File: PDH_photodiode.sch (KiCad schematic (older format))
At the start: 23 parts, among them J1 CONN_01X03, J2 CONN_01X02, U1 LT3032-5, U2 LTC6269

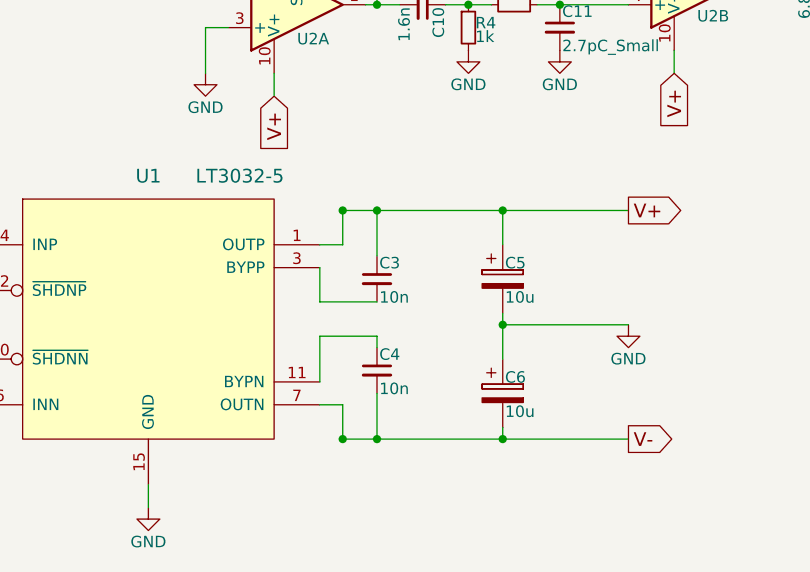
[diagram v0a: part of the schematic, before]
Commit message: LT3032
Replaced LT3032-05 with variable version
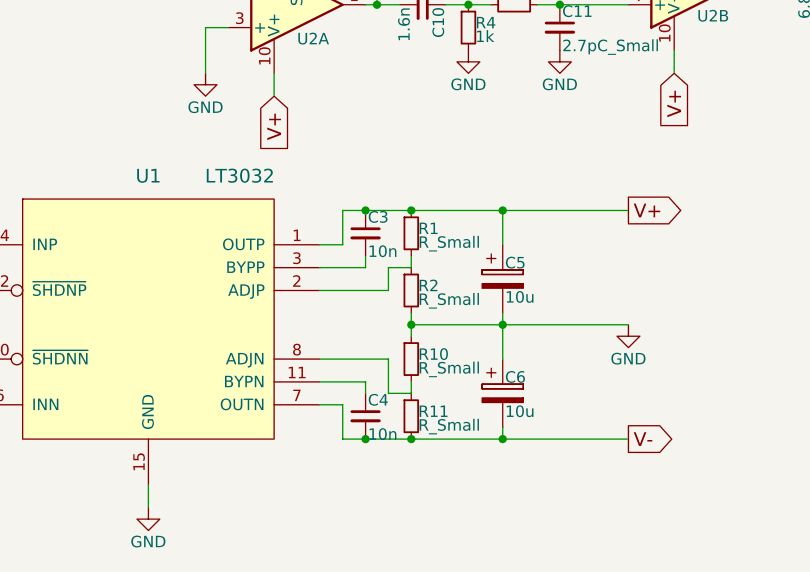
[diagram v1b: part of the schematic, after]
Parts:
- removed U1: LT3032-5, custom_Patrick_Baus:DFN-14-1EP_3x4mm_Pitch0.5mm_2Pads, symbol LT3032-X
- added R1, R10, R11, R2: R_Small, Resistors_SMD:R_0603, symbol R_Small
- added U1: LT3032, symbol LT3032
- U2: footprint Housings_DFN_QFN:DFN-10-1EP_3x3mm_Pitch0.5mm -> (none)
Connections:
- net GND: now also R10.1, R2.2, U1.15 (GND), U1.4, U1.5
- net INN: now also U1.10 (~SHDNN), U1.16 (INN), U1.6 (INN), U1.9 (INN)
- net V+: now also R1.1, U1.1 (OUTP)
- net V-: now also R11.2, U1.7 (OUTN)
- net at C1.1, J1.1 (P1): now also U1.12 (~SHDNP), U1.14 (INP)
- net at C3.2: now also U1.3 (BYPP)
- net at C4.1: now also U1.11 (BYPN)
- new net: R1.2, R2.1, U1.2 (ADJP)
- new net: R10.2, R11.1, U1.8 (ADJN)
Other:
- moved on the sheet: C3, C4

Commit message: Revision 1.1
-Add DC output
-Fit board in a box
  (RND 455-00367)
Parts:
- removed C10: 1.6n, Capacitors_SMD:C_0805, symbol C_Small
- removed C11: 2.7pC_Small, Capacitors_SMD:C_0805, symbol C_Small
- removed C12: 6.8n, Capacitors_SMD:C_0805, symbol C_Small
- removed C13: 75p, Capacitors_SMD:C_0805, symbol C_Small
- removed C5, C6: 10u, Capacitors_Tantalum_SMD:CP_Tantalum_Case-D_EIA-7343-31_Reflow, symbol CP
- removed D1: S9055, PDH_photodiode:PhotoDiode_S9055, symbol S9055
- removed R1, R10, R11, R2: R_Small, Resistors_SMD:R_0603, symbol R_Small
- removed R4, R5: 1k, Resistors_SMD:R_0805, symbol R_Small
- removed R6: 100, Resistors_SMD:R_0603, symbol R_Small
- removed R7: 910, Resistors_SMD:R_0603, symbol R_Small
- removed R8, R9: 49.9, Resistors_SMD:R_0805, symbol R_Small
- removed U1: LT3032, symbol LT3032
- removed U2: LTC6269, symbol LTC6269
- added C10, C11, C8: DNF, Capacitor_SMD:C_0603_1608Metric, symbol Device:C_Small
- added C12: 100n, Capacitor_SMD:C_0603_1608Metric, symbol Device:C_Small
- added C5, C6: 10u, Capacitor_SMD:C_1210_3225Metric, symbol Device:C_Small
- added C7: 1.6n/C0G, Capacitor_SMD:C_0603_1608Metric, symbol Device:C_Small
- added D1: S9055, footprints:TO-18-3_mod, symbol Sensor_Optical:S5971
- added H1, H2: MountingHole, MountingHole:MountingHole_4.3mm_M4_DIN965, symbol Mechanical:MountingHole
- added J3: DC Out, Connector_Coaxial:SMA_Amphenol_901-144_Vertical, symbol Connector:Conn_Coaxial
- added LOGO1: Logo_APQ, footprints:APQ-Logo, symbol Custom_logos:Logo_APQ
- added LOGO2: Logo_ROHS, Symbol:RoHS-Logo_6mm_SilkScreen, symbol Custom_logos:Logo_ROHS
- added LOGO3: Logo_Open_Hardware_Small, Symbol:OSHW-Logo_5.7x6mm_SilkScreen, symbol Graphic:Logo_Open_Hardware_Small
- added R1: 1k, Resistor_SMD:R_0603_1608Metric, symbol Device:R_Small
- added R10: 200, Resistor_SMD:R_0603_1608Metric, symbol Device:R_Small
- added R11, R4: 49.9, Resistor_SMD:R_1206_3216Metric, symbol Device:R_Small
- added R2, R7: 105k, Resistor_SMD:R_0603_1608Metric, symbol Device:R_Small
- added R5, R6: 100k, Resistor_SMD:R_0603_1608Metric, symbol Device:R_Small
- added R8: 0, Resistor_SMD:R_0603_1608Metric, symbol Device:R_Small
- added R9: 10, Resistor_SMD:R_0603_1608Metric, symbol Device:R_Small
- added U1: LT3032, Package_DFN_QFN:Linear_DE14MA, symbol Regulator_Linear:LT3032
- added U2: LTC6269-10, Package_DFN_QFN:DFN-10-1EP_3x3mm_P0.5mm_EP1.65x2.38mm, symbol Amplifier_Operational:LTC6229xDD
- C1, C2: footprint Capacitors_SMD:C_1210 -> Capacitor_SMD:C_1210_3225Metric; symbol C_Small -> Device:C_Small; MFN (none) -> Taiyo Yuden; PN (none) -> GMK325BJ106MN-T
- C3, C4: footprint Capacitors_SMD:C_0603 -> Capacitor_SMD:C_0603_1608Metric; symbol C_Small -> Device:C_Small; MFN (none) -> Murata Electronics; PN (none) -> GRM1885C1H103JA01D
- C9: footprint Capacitors_SMD:C_1206 -> Capacitor_SMD:C_0603_1608Metric; symbol C_Small -> Device:C_Small; MFN (none) -> Wurth Electronics; PN (none) -> 885012206071
- J1: value CONN_01X03 -> ±5V-Supply; footprint Pin_Headers:Pin_Header_Straight_1x03_Pitch2.54mm -> Connector_PinHeader_2.54mm:PinHeader_1x03_P2.54mm_Vertical; symbol CONN_01X03 -> Connector_Generic:Conn_01x03; Config (none) -> DNF
- J2: value CONN_01X02 -> AC Out; footprint Connectors:SMA_THT_Jack_Straight -> Connector_Coaxial:SMA_Amphenol_132203-12_Horizontal; symbol CONN_01X02 -> Connector:Conn_Coaxial; Config (none) -> DNF; MFN (none) -> Amphenol; PN (none) -> 901-143-6RFX
- R3: value 50k -> 10k; footprint Resistors_SMD:R_0603 -> footprints:R_0603_1608Metric_mod; symbol R_Small -> Device:R_Small; MFN (none) -> Susumu
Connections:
- net GND: now also C10.2, C11.2, C12.1, C5.2, C6.1, C8.2, D1.2 (C), J3.2 (Ext), R1.1, R5.2, R6.1, R9.1, U1.4 (GND), U1.5 (GND), U2.2 (-)
- net V+: now also C12.2, C5.1, R2.1, U1.1 (OUTP), U2.10 (V+)
- net V-: now also C6.2, D1.3 (A), R7.2, U1.7 (OUTN), U2.11 (V-), U2.4 (V-)
- net at C1.1, J1.1 (Pin_1): now also U1.12 (~SHDNP), U1.14 (INP)
- net at C3.2: now also U1.3 (BYPP)
- net at C4.1: now also U1.11 (BYPN)
- net at J2.1 (In): now also C10.1, R4.1
- net at R3.1: now also C7.2, R11.2, U2.1
- net at R3.2: now also D1.1 (K), U2.3 (+)
- net INN: no longer names the net of C2.2, J1.3 (Pin_3)
- net INN: now also U1.10 (~SHDNN), U1.6 (INN), U1.9 (INN)
- new net: R10.2, R4.2, U2.9
- new net: R2.2, R5.1, U1.2 (ADJP)
- new net: R6.2, R7.1, U1.8 (ADJN)
- new net: C8.1, R8.2, U2.7 (+)
- new net: R10.1, R9.2, U2.8 (-)
- new net: C7.1, R1.2, R8.1
- new net: C11.1, J3.1 (In), R11.1
- no-connect marks 0 -> 2
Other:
- note added: "See README for alternative gain (R3)"
- note added: "The footprint pad size for D1 and R3 has been reduced\nin order to reduce parasitic capacitance. Do not use too much solder paste \nand clean carefully after assembly.\n"
- note added: "Use C8 (and R8) and C10 (and R4)\nfor optional low pass filtering."
- moved on the sheet: C1, C2, C3, C4, C9, R3

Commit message: Add README
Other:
- note added: "Use C1 (and R11) for \noptional low pass filtering."
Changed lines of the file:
@@
 NoConn ~ 4600 2650
 NoConn ~ 7850 2750
+Text Notes 6300 900  0    60   ~ 0
+Use C1 (and R11) for \noptional low pass filtering.
 $EndSCHEMATC

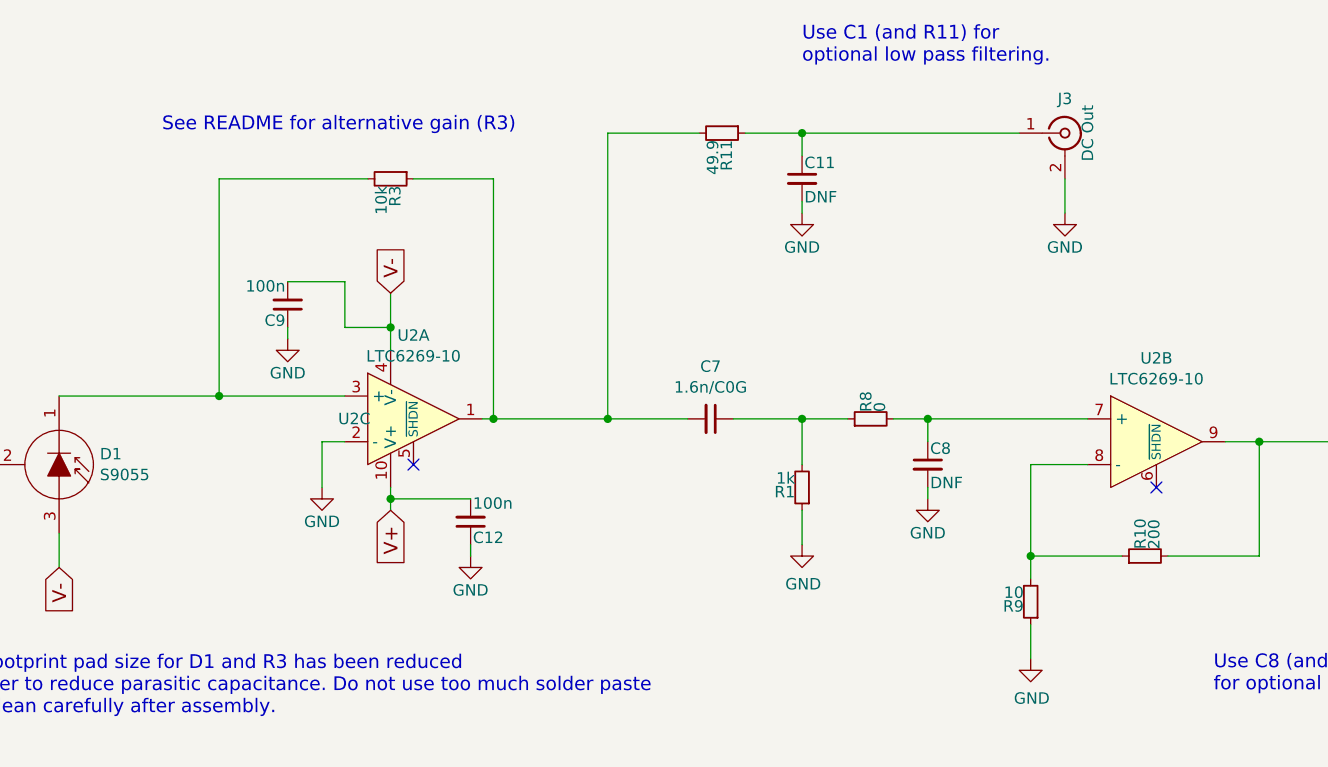
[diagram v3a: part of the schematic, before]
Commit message: Fix: Swap inverting and non-inverting input of TIA
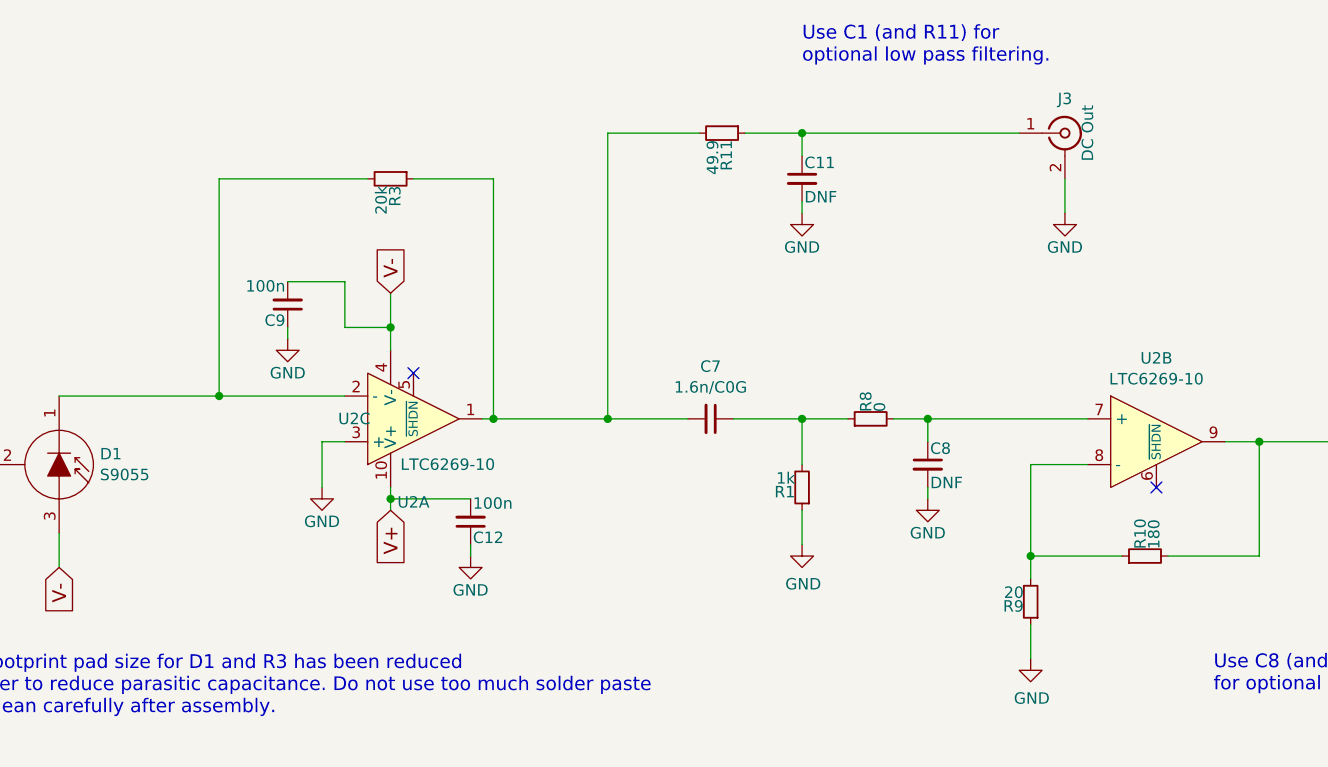
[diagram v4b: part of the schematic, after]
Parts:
- R10: value 200 -> 180
- R3: value 10k -> 20k
- R9: value 10 -> 20
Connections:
- net GND: now also U2.3 (+); no longer U2.2 (-)
- net at D1.1 (K), R3.2: now also U2.2 (-); no longer U2.3 (+)
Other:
- note removed: "See README for alternative gain (R3)"
- moved on the sheet: U2A
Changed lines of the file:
@@
 P 4500 1400
 F 0 "R3" H 4530 1420 50  0000 L CNN
-F 1 "10k" H 4530 1360 50  0000 L CNN
+F 1 "20k" H 4530 1360 50  0000 L CNN
 F 2 "footprints:R_0603_1608Metric_mod" H 4500 1400 50  0001 C CNN
 F 3 "" H 4500 1400 50  0001 C CNN
@@
 P 4600 2450
 F 0 "U2" H 4600 2815 50  0000 C CNN
-F 1 "LTC6269-10" H 4600 2724 50  0000 C CNN
+F 1 "LTC6269-10" H 4750 2650 50  0000 C CNN
 F 2 "Package_DFN_QFN:DFN-10-1EP_3x3mm_P0.5mm_EP1.65x2.38mm" H 4600 2050 50  0001 C CNN
 F 3 "" H 4600 2450 50  0001 C CNN
 	1    4600 2450
-	1    0    0    -1
+	1    0    0    1
 $EndComp
 $Comp
@@
 P 7300 3250
 F 0 "R9" H 7330 3270 50  0000 L CNN
-F 1 "10" H 7330 3210 50  0000 L CNN
+F 1 "20" H 7330 3210 50  0000 L CNN
 F 2 "Resistor_SMD:R_0603_1608Metric" H 7300 3250 50  0001 C CNN
 F 3 "" H 7300 3250 50  0001 C CNN
@@
 P 7800 3050
 F 0 "R10" H 7830 3070 50  0000 L CNN
-F 1 "200" H 7830 3010 50  0000 L CNN
+F 1 "180" H 7830 3010 50  0000 L CNN
 F 2 "Resistor_SMD:R_0603_1608Metric" H 7800 3050 50  0001 C CNN
 F 3 "" H 7800 3050 50  0001 C CNN
@@
 Text Notes 2550 3750 0    60   ~ 0
 The footprint pad size for D1 and R3 has been reduced\nin order to reduce parasitic capacitance. Do not use too much solder paste  \nand clean carefully after assembly.\n
-Text Notes 3500 1200 0    60   ~ 0
-See README for alternative gain (R3)
 Wire Wire Line
 	4500 2800 4850 2800
-NoConn ~ 4600 2650
+NoConn ~ 4600 2250
 NoConn ~ 7850 2750
 Text Notes 6300 900  0    60   ~ 0

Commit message: Update BOM and gerber files
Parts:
- C1, C2, C5, C6: PN GMK325BJ106MN-T -> UMR325AC7106MM-P
- C7: value 1.6n/C0G -> 10n; MFN (none) -> Murata Electronics; PN (none) -> GRM1885C1H103JA01D
- D1: Config (none) -> DNF
- J2: Config DNF -> (none)
- R1: MFN Susumu -> Yageo; PN (none) -> RT0603DRE071KL
- R10: PN (none) -> RR0816P-181-D
- R2, R7: MFN (none) -> Susumu; PN (none) -> RR0816P-1053-D-03D
- R3: PN (none) -> RR0816P-203-D
- R5, R6: MFN (none) -> Susumu; PN (none) -> RR0816P-104-D
- R8: MFN Susumu -> Vishay/Beyschlag; PN (none) -> MCT06030Z0000ZP500
- R9: PN (none) -> RR0816Q-200-D
- U1: MFN (none) -> Analog Devices; PN (none) -> LT3032EDE#PBF
- U2: MFN (none) -> Analog Devices; PN (none) -> LTC6269HDD-10#PBF
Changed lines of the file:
@@
 F 3 "" H 4000 4750 50  0001 C CNN
 F 4 "Taiyo Yuden" H 4000 4750 60  0001 C CNN "MFN"
-F 5 "GMK325BJ106MN-T" H 4000 4750 50  0001 C CNN "PN"
+F 5 "UMR325AC7106MM-P" H 4000 4750 50  0001 C CNN "PN"
 	1    4000 4750
 	1    0    0    -1
@@
 F 3 "" H 4000 5450 50  0001 C CNN
 F 4 "Taiyo Yuden" H 4000 5450 60  0001 C CNN "MFN"
-F 5 "GMK325BJ106MN-T" H 4000 5450 50  0001 C CNN "PN"
+F 5 "UMR325AC7106MM-P" H 4000 5450 50  0001 C CNN "PN"
 	1    4000 5450
 	1    0    0    -1
@@
 F 3 "" H 4500 1400 50  0001 C CNN
 F 4 "Susumu" H 4500 1400 60  0001 C CNN "MFN"
-F 5 "" H 4500 1400 50  0001 C CNN "PN"
+F 5 "RR0816P-203-D" H 4500 1400 50  0001 C CNN "PN"
 	1    4500 1400
 	0    1    1    0
@@
 F 3 "" H 6950 4900 50  0001 C CNN
 F 4 "Taiyo Yuden" H 6950 4900 60  0001 C CNN "MFN"
-F 5 "GMK325BJ106MN-T" H 6950 4900 50  0001 C CNN "PN"
+F 5 "UMR325AC7106MM-P" H 6950 4900 50  0001 C CNN "PN"
 	1    6950 4900
 	1    0    0    -1
@@
 F 3 "" H 6950 5400 50  0001 C CNN
 F 4 "Taiyo Yuden" H 6950 5400 60  0001 C CNN "MFN"
-F 5 "GMK325BJ106MN-T" H 6950 5400 50  0001 C CNN "PN"
+F 5 "UMR325AC7106MM-P" H 6950 5400 50  0001 C CNN "PN"
 	1    6950 5400
 	1    0    0    -1
@@
 F 2 "Package_DFN_QFN:Linear_DE14MA" H 5350 5025 50  0001 C CNN
 F 3 "https://www.analog.com/media/en/technical-documentation/data-sheets/3032ff.pdf" H 5350 4700 50  0001 C CNN
+F 4 "Analog Devices" H 5350 4700 50  0001 C CNN "MFN"
+F 5 "LT3032EDE#PBF" H 5350 4700 50  0001 C CNN "PN"
 	1    5350 4700
 	1    0    0    -1
@@
 F 2 "Package_DFN_QFN:Linear_DE14MA" H 5350 5825 50  0001 C CNN
 F 3 "https://www.analog.com/media/en/technical-documentation/data-sheets/3032ff.pdf" H 5350 5500 50  0001 C CNN
+F 4 "Analog Devices" H 5350 5500 50  0001 C CNN "MFN"
+F 5 "LT3032EDE#PBF" H 5350 5500 50  0001 C CNN "PN"
 	2    5350 5500
 	1    0    0    1
@@
 F 2 "Resistor_SMD:R_0603_1608Metric" H 6450 4700 50  0001 C CNN
 F 3 "~" H 6450 4700 50  0001 C CNN
+F 4 "Susumu" H 6450 4700 50  0001 C CNN "MFN"
+F 5 "RR0816P-1053-D-03D" H 6450 4700 50  0001 C CNN "PN"
 	1    6450 4700
 	1    0    0    -1
@@
 F 2 "Resistor_SMD:R_0603_1608Metric" H 6450 5000 50  0001 C CNN
 F 3 "~" H 6450 5000 50  0001 C CNN
+F 4 "Susumu" H 6450 5000 50  0001 C CNN "MFN"
+F 5 "RR0816P-104-D" H 6450 5000 50  0001 C CNN "PN"
 	1    6450 5000
 	1    0    0    -1
@@
 F 2 "Resistor_SMD:R_0603_1608Metric" H 6450 5500 50  0001 C CNN
 F 3 "~" H 6450 5500 50  0001 C CNN
+F 4 "Susumu" H 6450 5500 50  0001 C CNN "MFN"
+F 5 "RR0816P-1053-D-03D" H 6450 5500 50  0001 C CNN "PN"
 	1    6450 5500
 	1    0    0    -1
@@
 F 2 "Resistor_SMD:R_0603_1608Metric" H 6450 5200 50  0001 C CNN
 F 3 "~" H 6450 5200 50  0001 C CNN
+F 4 "Susumu" H 6450 5200 50  0001 C CNN "MFN"
+F 5 "RR0816P-104-D" H 6450 5200 50  0001 C CNN "PN"
 	1    6450 5200
 	1    0    0    -1
@@
 F 4 "Hamamatsu" V 3050 2650 50  0001 C CNN "MFN"
 F 5 "S9055-01" V 3050 2650 50  0001 C CNN "PN"
+F 6 "DNF" V 3050 2650 50  0001 C CNN "Config"
 	1    3050 2650
 	0    1    1    0
@@
 F 2 "Package_DFN_QFN:DFN-10-1EP_3x3mm_P0.5mm_EP1.65x2.38mm" H 4600 2050 50  0001 C CNN
 F 3 "" H 4600 2450 50  0001 C CNN
+F 4 "Analog Devices" H 4600 2450 50  0001 C CNN "MFN"
+F 5 "LTC6269HDD-10#PBF" H 4600 2450 50  0001 C CNN "PN"
 	1    4600 2450
 	1    0    0    1
@@
 F 2 "Package_DFN_QFN:DFN-10-1EP_3x3mm_P0.5mm_EP1.65x2.38mm" H 7850 2150 50  0001 C CNN
 F 3 "" H 7850 2550 50  0001 C CNN
+F 4 "Analog Devices" H 7850 2550 50  0001 C CNN "MFN"
+F 5 "LTC6269HDD-10#PBF" H 7850 2550 50  0001 C CNN "PN"
 	2    7850 2550
 	1    0    0    -1
@@
 P 5900 2450
 F 0 "C7" V 5671 2450 50  0000 C CNN
-F 1 "1.6n/C0G" V 5762 2450 50  0000 C CNN
+F 1 "10n" V 5762 2450 50  0000 C CNN
 F 2 "Capacitor_SMD:C_0603_1608Metric" H 5900 2450 50  0001 C CNN
 F 3 "~" H 5900 2450 50  0001 C CNN
+F 4 "Murata Electronics" V 5900 2450 50  0001 C CNN "MFN"
+F 5 "GRM1885C1H103JA01D" V 5900 2450 50  0001 C CNN "PN"
 	1    5900 2450
 	0    1    1    0
@@
 F 2 "Resistor_SMD:R_0603_1608Metric" H 6300 2750 50  0001 C CNN
 F 3 "" H 6300 2750 50  0001 C CNN
-F 4 "Susumu" H 6300 2750 60  0001 C CNN "MFN"
-F 5 "" H 6300 2750 50  0001 C CNN "PN"
+F 4 "Yageo" H 6300 2750 60  0001 C CNN "MFN"
+F 5 "RT0603DRE071KL" H 6300 2750 50  0001 C CNN "PN"
 	1    6300 2750
 	-1   0    0    1
@@
 F 3 "" H 7300 3250 50  0001 C CNN
 F 4 "Susumu" H 7300 3250 60  0001 C CNN "MFN"
-F 5 "" H 7300 3250 50  0001 C CNN "PN"
+F 5 "RR0816Q-200-D" H 7300 3250 50  0001 C CNN "PN"
 	1    7300 3250
 	-1   0    0    1
@@
 F 3 "" H 7800 3050 50  0001 C CNN
 F 4 "Susumu" H 7800 3050 60  0001 C CNN "MFN"
-F 5 "" H 7800 3050 50  0001 C CNN "PN"
+F 5 "RR0816P-181-D" H 7800 3050 50  0001 C CNN "PN"
 	1    7800 3050
 	0    -1   -1   0
@@
 F 2 "Resistor_SMD:R_0603_1608Metric" H 6600 2450 50  0001 C CNN
 F 3 "" H 6600 2450 50  0001 C CNN
-F 4 "Susumu" H 6600 2450 60  0001 C CNN "MFN"
-F 5 "" H 6600 2450 50  0001 C CNN "PN"
+F 4 "Vishay/Beyschlag" H 6600 2450 60  0001 C CNN "MFN"
+F 5 "MCT06030Z0000ZP500" H 6600 2450 50  0001 C CNN "PN"
 	1    6600 2450
 	0    -1   -1   0
@@
 F 4 "Amphenol" H 10400 2550 50  0001 C CNN "MFN"
 F 5 "901-143-6RFX" H 10400 2550 50  0001 C CNN "PN"
-F 6 "DNF" H 10400 2550 50  0001 C CNN "Config"
+F 6 "" H 10400 2550 50  0001 C CNN "Config"
 	1    10400 2550
 	1    0    0    -1
